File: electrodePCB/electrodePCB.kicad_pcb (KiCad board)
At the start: 2 copper layers, 58 x 58 mm, 17 parts, among them J1 Conn_01x16_Pin, U1 TMP119AIYBGR

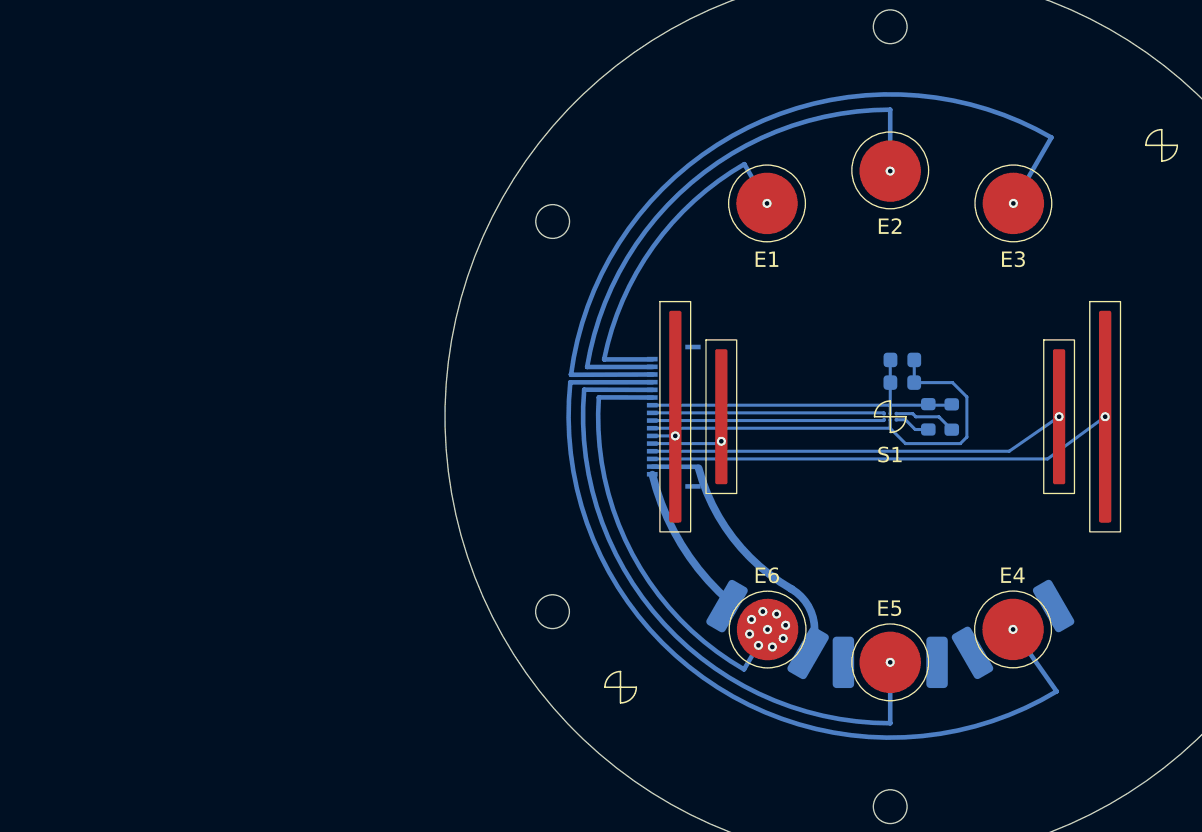
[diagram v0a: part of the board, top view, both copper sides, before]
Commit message: still in the middle of it, but added the 20p, 2 additional heaters (including adjustable postition) and begining to define pinout
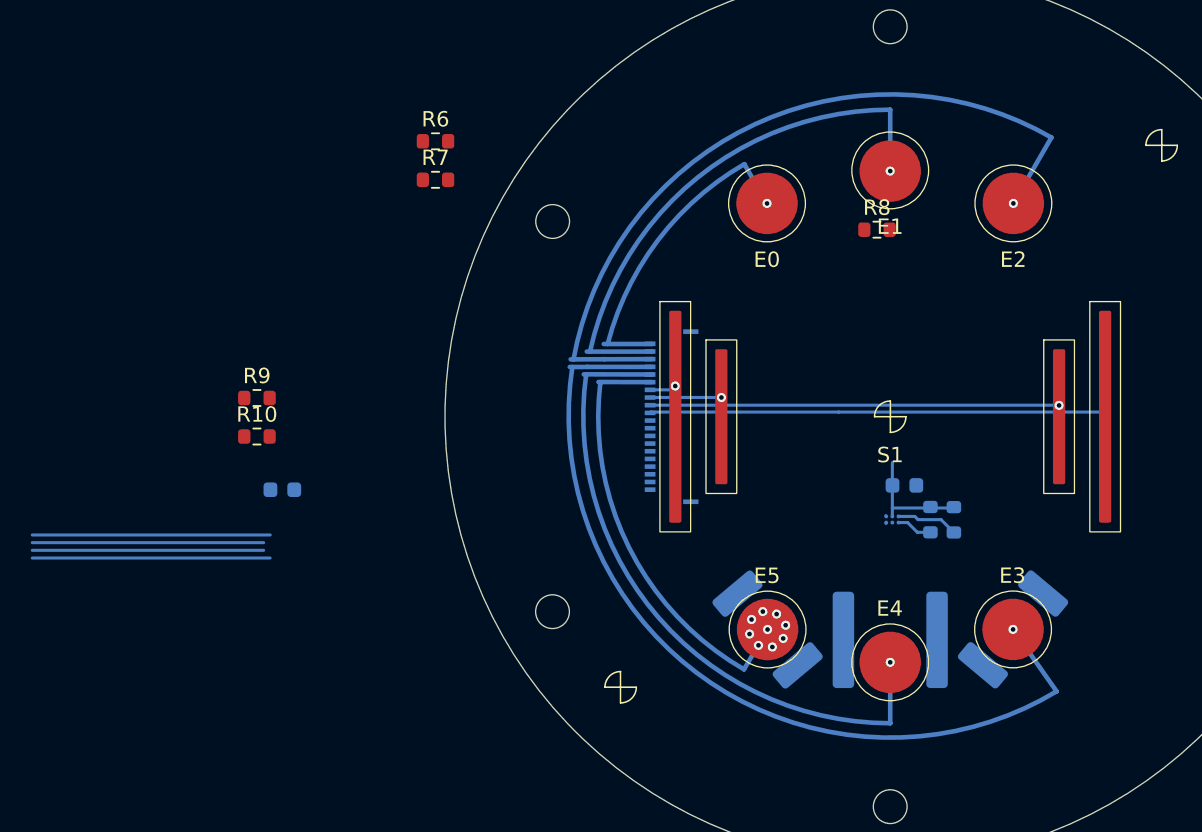
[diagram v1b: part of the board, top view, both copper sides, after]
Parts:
- removed the R1 at (100.0, 116.0)
- removed the R1 at (108.0, 113.9)
- added R10: R_US, Resistor_SMD:R_0603_1608Metric, F.Cu at (58.7, 101.3)
- added R2: R_Small_US, Resistor_SMD:adjustable, B.Cu at (100.0, 116.0)
- added R3: R_Small_US, Resistor_SMD:R_2512_6332Metric_Pad1.40x3.35mm_HandSolder, B.Cu at (108.0, 113.9)
- added R6: R_US, Resistor_SMD:R_0603_1608Metric, F.Cu at (70.4, 82.1)
- added R7: R_US, Resistor_SMD:R_0603_1608Metric, F.Cu at (70.4, 84.6)
- added R8: R_US, Resistor_SMD:R_0603_1608Metric, F.Cu at (99.1, 87.8)
- added R9: R_US, Resistor_SMD:R_0603_1608Metric, F.Cu at (58.7, 98.8)
- J1: value Conn_01x16_Pin -> Conn_01x20; footprint MOLEX FPC:CON_5034801600_MOL -> 5034802000 FPC Molex:CON_5034802000_MOL
- moved C2 41.3 mm to (60.4, 104.8)
- moved C1 6.70 mm to (100.9, 104.5)
- moved R4 6.70 mm to (102.6, 106.7)
- moved R5 6.70 mm to (104.1, 106.7)
- moved U1 6.70 mm to (100.1, 106.7)
- moved J1 0.14 mm to (85.9, 100.0)
- turned R1 to -50 degrees
- renumbered E1 to E0, E2 to E1, E3 to E2, E4 to E3, E5 to E4, E6 to E5, R3 to R4, R2 to R5
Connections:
- J1 pad 10: GND -> Net-(J1-Pin_10)
- J1 pad 11: Net-(J1-Pin_11) -> +3V3
- J1 pad 12: Net-(J1-Pin_12) -> SDA
- J1 pad 13: Net-(J1-Pin_13) -> SCL
- J1 pad 14: Net-(J1-Pin_14) -> GND
- J1 pad 15: Net-(J1-Pin_15) -> GND
- J1 pad 7: +3V3 -> Net-(J1-Pin_7)
- J1 pad 8: SDA -> Net-(J1-Pin_8)
- J1 pad 9: SCL -> Net-(J1-Pin_9)
- R1 pad 1: Net-(J1-Pin_15) -> Net-(J1-Pin_20)
- R1 pad 2: Net-(J1-Pin_16) -> GND
- S1 pad 1: Net-(J1-Pin_11) -> Net-(J1-Pin_7)
- S1 pad 2: Net-(J1-Pin_12) -> Net-(J1-Pin_8)
- S1 pad 3: Net-(J1-Pin_13) -> Net-(J1-Pin_9)
- S1 pad 4: Net-(J1-Pin_14) -> Net-(J1-Pin_10)
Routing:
- net Net-(J1-Pin_14): track 30.4 -> 0.00 mm, vias 1 -> 0
- net Net-(J1-Pin_10): track 0.00 -> 29.7 mm
- net Net-(J1-Pin_13): track 27.2 -> 0.00 mm, vias 1 -> 0
- net Net-(J1-Pin_9): track 0.00 -> 26.6 mm, vias 0 -> 1
- net GND: track 29.5 -> 15.5 mm
- net Net-(J1-Pin_8): track 0.00 -> 4.64 mm, vias 0 -> 1
- net Net-(J1-Pin_12): track 4.56 -> 0.00 mm, vias 1 -> 0
- net Net-(J1-Pin_7): track 0.00 -> 1.64 mm, vias 0 -> 1
- net Net-(J1-Pin_11): track 1.50 -> 0.00 mm, vias 1 -> 0

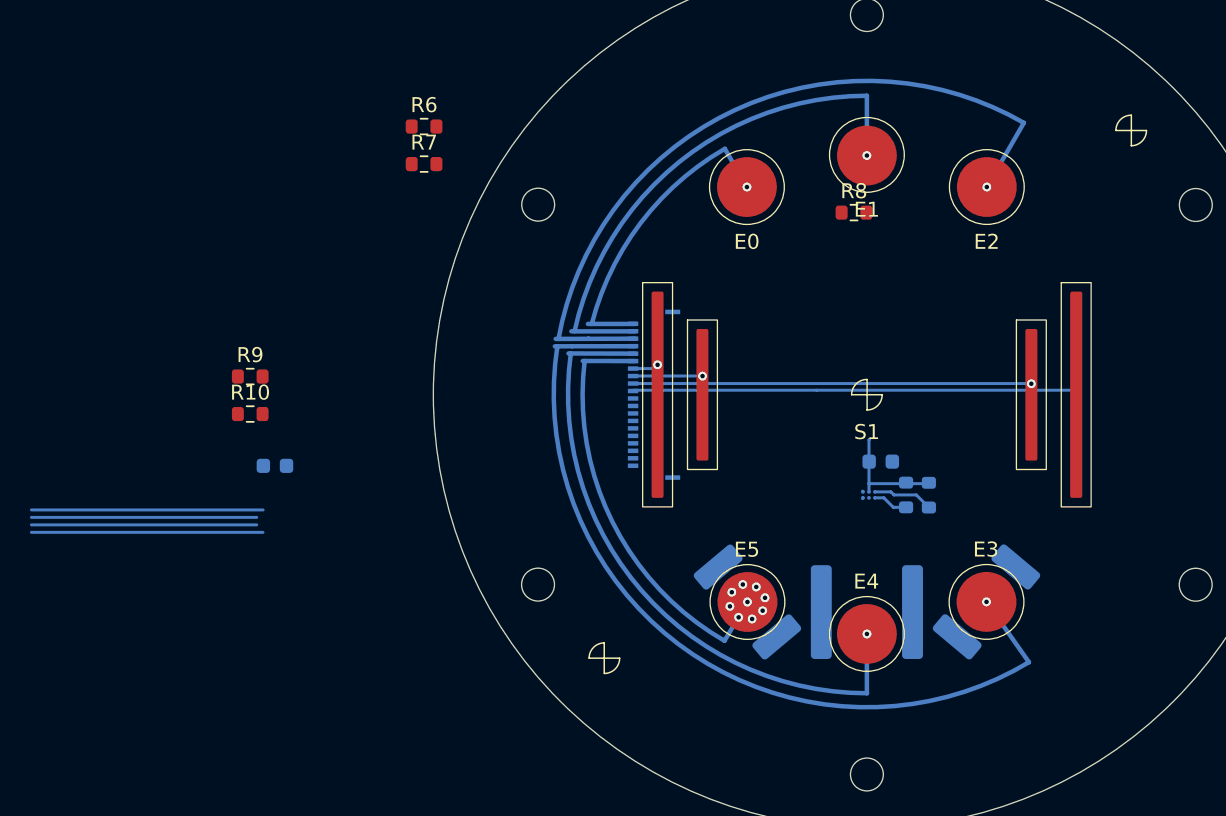
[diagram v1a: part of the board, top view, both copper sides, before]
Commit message: bunch of routing, adapted interconnect pinout to accomedate routing. Added GND plane.
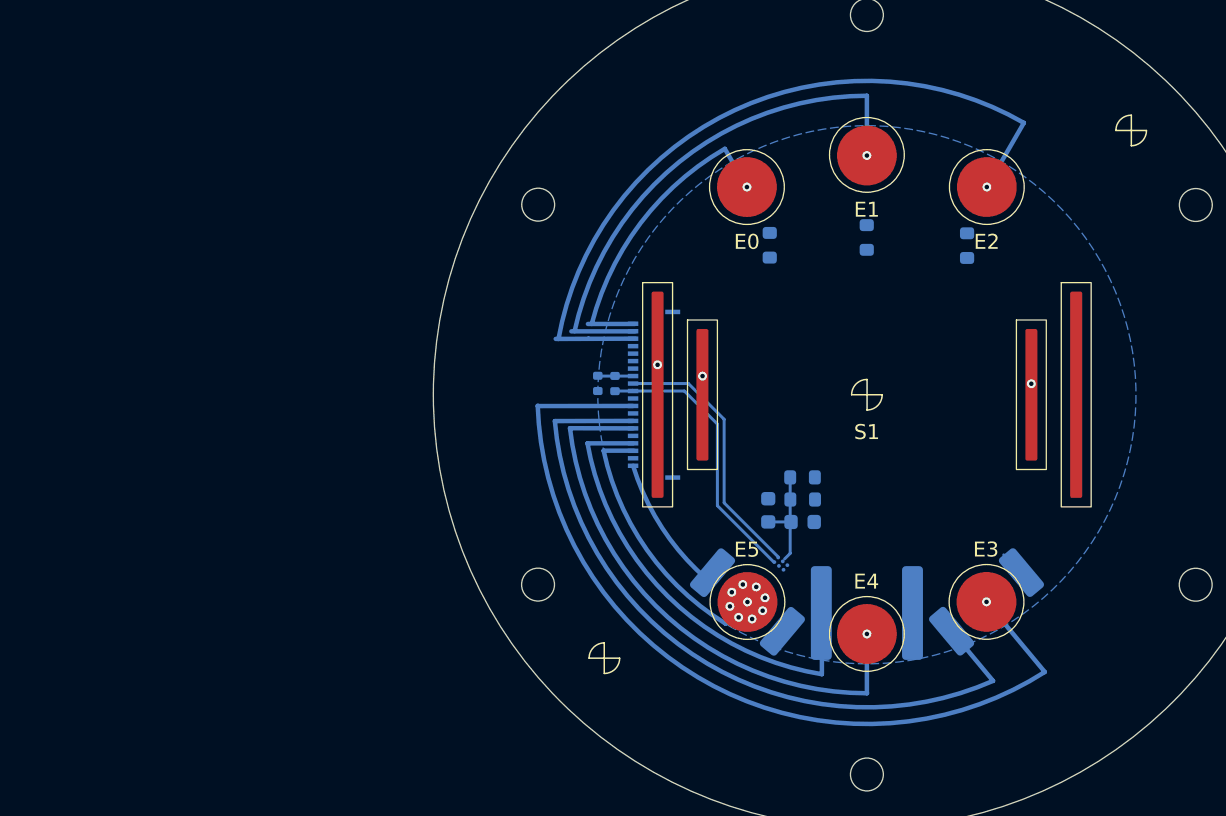
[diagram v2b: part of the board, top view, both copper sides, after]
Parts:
- R10, R8, R9: moved to B.Cu
- R6, R7: footprint Resistor_SMD:R_0603_1608Metric -> Resistor_SMD:R_0402_1005Metric; moved to B.Cu
- moved R10 49.3 mm to (106.7, 90.0), turned to 90 degrees
- moved R9 42.3 mm to (100.0, 89.5), turned to 90 degrees
- moved C2 33.1 mm to (93.4, 107.7), turned to 90 degrees
- moved R6 21.4 mm to (83.2, 99.2), turned to 90 degrees
- moved R7 18.7 mm to (82.0, 99.2), turned to -90 degrees
- moved R5 8.45 mm to (95.7, 107.0), turned to 0 degrees
- moved U1 7.48 mm to (94.2, 111.3), turned to -130 degrees
- moved R4 7.02 mm to (95.7, 105.5), turned to 180 degrees
- moved C1 6.60 mm to (95.7, 108.5)
- moved R8 6.04 mm to (93.5, 90.0), turned to 90 degrees
- moved R2 2.86 mm to (100.0, 113.1), turned to 0 degrees
- turned R1 to -40 degrees
- turned R3 to 40 degrees
- turned REF** to 10 degrees
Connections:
- J1 pad 10: Net-(J1-Pin_10) -> SCL
- J1 pad 11: +3V3 -> GND
- J1 pad 12: SDA -> Net-(E3-Pin_1)
- J1 pad 13: SCL -> GND
- J1 pad 14: GND -> Net-(J1-Pin_14)
- J1 pad 15: GND -> Net-(E4-Pin_1)
- J1 pad 16: Net-(J1-Pin_16) -> GND
- J1 pad 17: GND -> Net-(J1-Pin_17)
- J1 pad 18: Net-(J1-Pin_18) -> Net-(E5-Pin_1)
- J1 pad 4: Net-(E3-Pin_1) -> Net-(J1-Pin_4)
- J1 pad 5: Net-(E4-Pin_1) -> Net-(J1-Pin_5)
- J1 pad 6: Net-(E5-Pin_1) -> Net-(J1-Pin_6)
- J1 pad 8: Net-(J1-Pin_8) -> +3V3
- J1 pad 9: Net-(J1-Pin_9) -> SDA
- R1 pad 1: Net-(J1-Pin_20) -> Net-(J1-Pin_14)
- R2 pad 1: Net-(J1-Pin_18) -> Net-(J1-Pin_17)
- R3 pad 1: Net-(J1-Pin_16) -> Net-(J1-Pin_20)
- S1 pad 1: Net-(J1-Pin_7) -> Net-(J1-Pin_4)
- S1 pad 2: Net-(J1-Pin_8) -> Net-(J1-Pin_5)
- S1 pad 3: Net-(J1-Pin_9) -> Net-(J1-Pin_6)
- S1 pad 4: Net-(J1-Pin_10) -> Net-(J1-Pin_7)
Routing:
- net Net-(J1-Pin_10): track 29.7 -> 0.00 mm
- net Net-(J1-Pin_9): track 26.6 -> 0.00 mm, vias 1 -> 0
- net GND: track 15.5 -> 1.68 mm
- net +3V3: track 23.0 -> 9.53 mm
- net Net-(J1-Pin_8): track 4.64 -> 0.00 mm, vias 1 -> 0
- net Net-(U1-ADD0): track 4.04 -> 0.00 mm
- net SCL: track 15.1 -> 18.6 mm
- net SDA: track 15.1 -> 17.5 mm
- net Net-(U1-ALERT): track 2.34 -> 0.00 mm
- net Net-(J1-Pin_7): track 1.64 -> 0.00 mm, vias 1 -> 0
- net Net-(J1-Pin_6): vias 0 -> 1
- net Net-(J1-Pin_4): vias 0 -> 1
- net Net-(J1-Pin_5): vias 0 -> 1
- added copper zone on B.Cu, net GND

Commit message: routing, routing, routing. We removed one of the three heaters and decided to displace the other two and route to rings around the electrodes. I verified the temperature sensor is work!
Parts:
- removed REF**: thermal_pad, Electrodes:thermal_pad
- added J2: qwiic, Connector_JST:JST_SH_BM04B-SRSS-TB_1x04-1MP_P1.00mm_Vertical, B.Cu at (72.4, 121.6)
- J1: value Conn_01x20 -> FPC 20p
- R1, R3: footprint Resistor_SMD:R_2512_6332Metric_Pad1.40x3.35mm_HandSolder -> Resistor_SMD:R_2010_5025Metric
- R2: footprint Resistor_SMD:adjustable -> Resistor_SMD:R_2010_5025Metric; moved to F.Cu
- moved R2 147.7 mm to (3.21, 1.60)
- moved U1 18.4 mm to (106.2, 97.4)
- moved R5 10.4 mm to (104.3, 101.1)
- moved R4 9.59 mm to (101.7, 98.0)
- moved C1 7.88 mm to (97.4, 100.8), turned to 90 degrees
- moved C2 7.38 mm to (95.9, 100.8)
- moved R3 3.96 mm to (105.6, 110.7)
- moved R1 3.84 mm to (94.5, 110.9)
- moved R9 3.54 mm to (100.8, 86.0), turned to 180 degrees
- moved R8 2.62 mm to (93.7, 87.4), turned to -150 degrees
- moved R10 2.06 mm to (107.8, 88.2), turned to 150 degrees
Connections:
- J1 pad 12: Net-(E3-Pin_1) -> unconnected-(J1-Pin_12-Pad12)
- J1 pad 13: GND -> unconnected-(J1-Pin_13-Pad13)
- J1 pad 14: Net-(J1-Pin_14) -> Net-(E3-Pin_1)
- J1 pad 15: Net-(E4-Pin_1) -> GND
- J1 pad 16: GND -> Net-(J1-Pin_16)
- J1 pad 17: Net-(J1-Pin_17) -> Net-(E4-Pin_1)
- J1 pad 18: Net-(E5-Pin_1) -> Net-(J1-Pin_18)
- J1 pad 20: Net-(J1-Pin_20) -> Net-(E5-Pin_1)
- R1 pad 1: Net-(J1-Pin_14) -> Net-(J1-Pin_18)
- R2 pad 1: Net-(J1-Pin_17) -> Net-(J1-Pin_18)
- R3 pad 1: Net-(J1-Pin_20) -> Net-(J1-Pin_16)
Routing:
- net SDA: track 17.5 -> 3.43 mm
- net SCL: track 18.6 -> 4.72 mm
- net Net-(E4-Pin_1): track 0.00 -> 6.02 mm
- net +3V3: track 9.53 -> 3.90 mm
- net GND: track 1.68 -> 0.02 mm
- net Net-(E5-Pin_1): vias 9 -> 1

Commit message: routing and more routing. still working, but add thermal rings. added qwiic.
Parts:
- removed C2: 10uF, Capacitor_SMD:C_0603_1608Metric
- R4, R5: footprint Resistor_SMD:R_0603_1608Metric -> Resistor_SMD:R_0402_1005Metric
- moved J2 44.4 mm to (113.5, 104.8), turned to 70 degrees
- moved R6 33.9 mm to (116.4, 105.9), turned to -110 degrees
- moved R7 27.2 mm to (108.9, 103.2), turned to 70 degrees
- moved U1 19.6 mm to (100.0, 116.0), turned to 0 degrees
- moved R4 17.5 mm to (98.8, 115.3), turned to -95 degrees
- moved R5 16.0 mm to (96.2, 114.9), turned to 75 degrees
- moved C1 13.9 mm to (97.6, 114.7), turned to 80 degrees
- moved J1 3.14 mm to (89.0, 100.0)
- moved R1 0.67 mm to (94.0, 110.4), turned to -30 degrees
- moved R3 0.49 mm to (106.0, 110.4), turned to 30 degrees
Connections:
- J1 pad 10: SCL -> +3V3
- J1 pad 8: +3V3 -> SCL
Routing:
- net SCL: track 4.72 -> 36.3 mm
- net +3V3: track 3.90 -> 33.4 mm
- net Net-(J1-Pin_7): track 0.00 -> 27.2 mm, vias 0 -> 1
- net SDA: track 3.43 -> 29.9 mm
- net Net-(J1-Pin_6): track 0.00 -> 23.5 mm
- net Net-(U1-ADD0): track 0.00 -> 4.36 mm
- net Net-(E0-Pin_1): track 0.00 -> 3.65 mm
- net Net-(E4-Pin_1): track 6.02 -> 3.65 mm
- net Net-(U1-ALERT): track 0.00 -> 1.72 mm
- net Net-(J1-Pin_5): track 0.00 -> 1.60 mm
- added copper zone on B.Cu, net (none)
- added copper zone on F.Cu, net (none)
- added copper zone on F.Cu, net unconnected-(J2-MountPin-PadMP)

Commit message: roughly finalized layout. Might tidy up the GND plane with some keep outs
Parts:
- removed the R2 at (3.21, 1.60)
- R1: renamed from R7; value R_US -> 10k
- R2: renamed from R6; value R_US -> 10k
- R4: value R_US -> 10k
- R6: renamed from R5; value R_US -> 10k
- renumbered R1 to R5, R8 to R7, R9 to R8, R10 to R9
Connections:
- J1 pad 12: unconnected-(J1-Pin_12-Pad12) -> Net-(E3-Pin_1)
- J1 pad 13: unconnected-(J1-Pin_13-Pad13) -> Net-(J1-Pin_13)
- J1 pad 14: Net-(E3-Pin_1) -> Net-(J1-Pin_13)
- J1 pad 16: Net-(J1-Pin_16) -> Net-(E4-Pin_1)
- J1 pad 17: Net-(E4-Pin_1) -> Net-(J1-Pin_17)
- J1 pad 18: Net-(J1-Pin_18) -> Net-(J1-Pin_17)
- J1 pad P1: (no net) -> GND
- J1 pad P2: (no net) -> GND
- R3 pad 1: Net-(J1-Pin_16) -> Net-(J1-Pin_13)
- R5 pad 1: Net-(J1-Pin_18) -> Net-(J1-Pin_17)
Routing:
- net Net-(U1-ADD0): track 4.36 -> 3.82 mm
- net E5_therm_pad: vias 0 -> 3
- net E3_therm_pad: vias 0 -> 3
- added copper zone on B.Cu, net E3_therm_pad
- added copper zone on F.Cu, net E3_therm_pad
- added copper zone on B.Cu, net E5_therm_pad
- added copper zone on F.Cu, net E5_therm_pad
- removed copper zone on B.Cu, net (none)
- removed copper zone on F.Cu, net (none)
- removed copper zone on F.Cu, net unconnected-(J2-MountPin-PadMP)

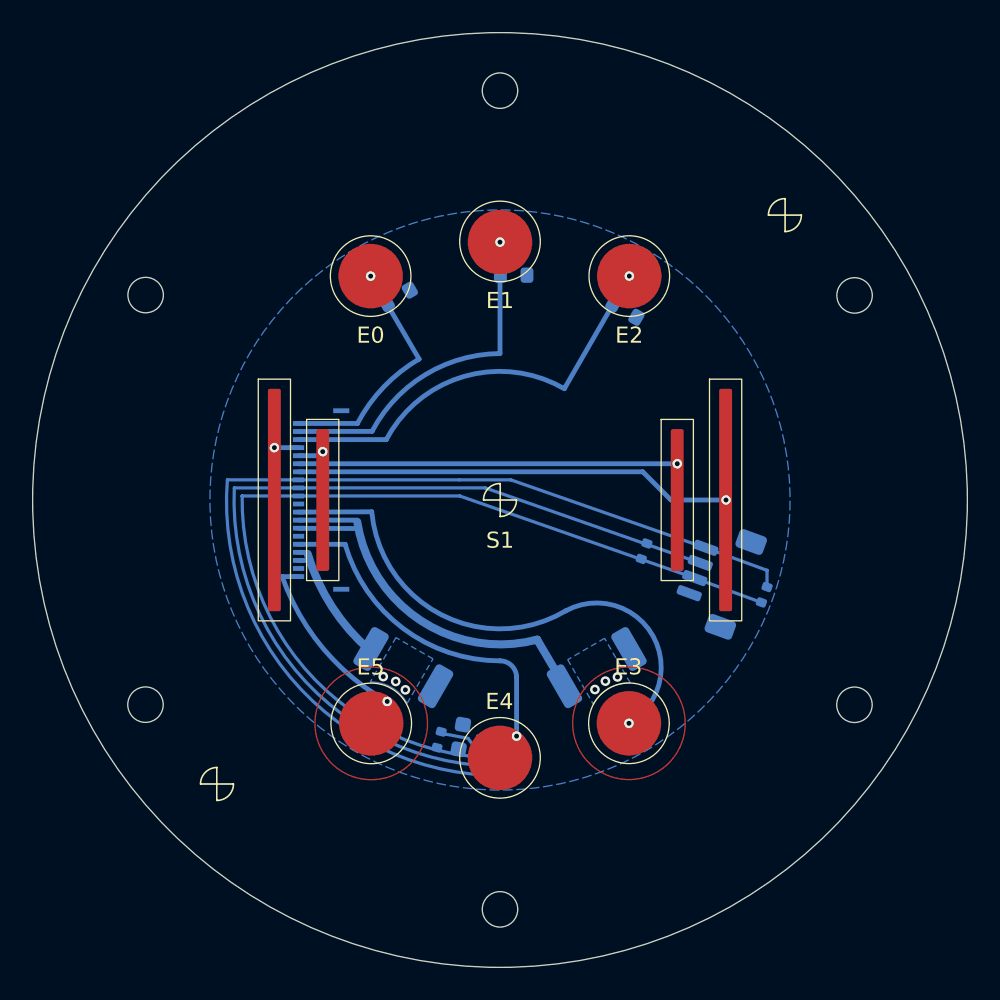
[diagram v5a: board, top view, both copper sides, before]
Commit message: added releifs for screws so we do not have to completely remove them
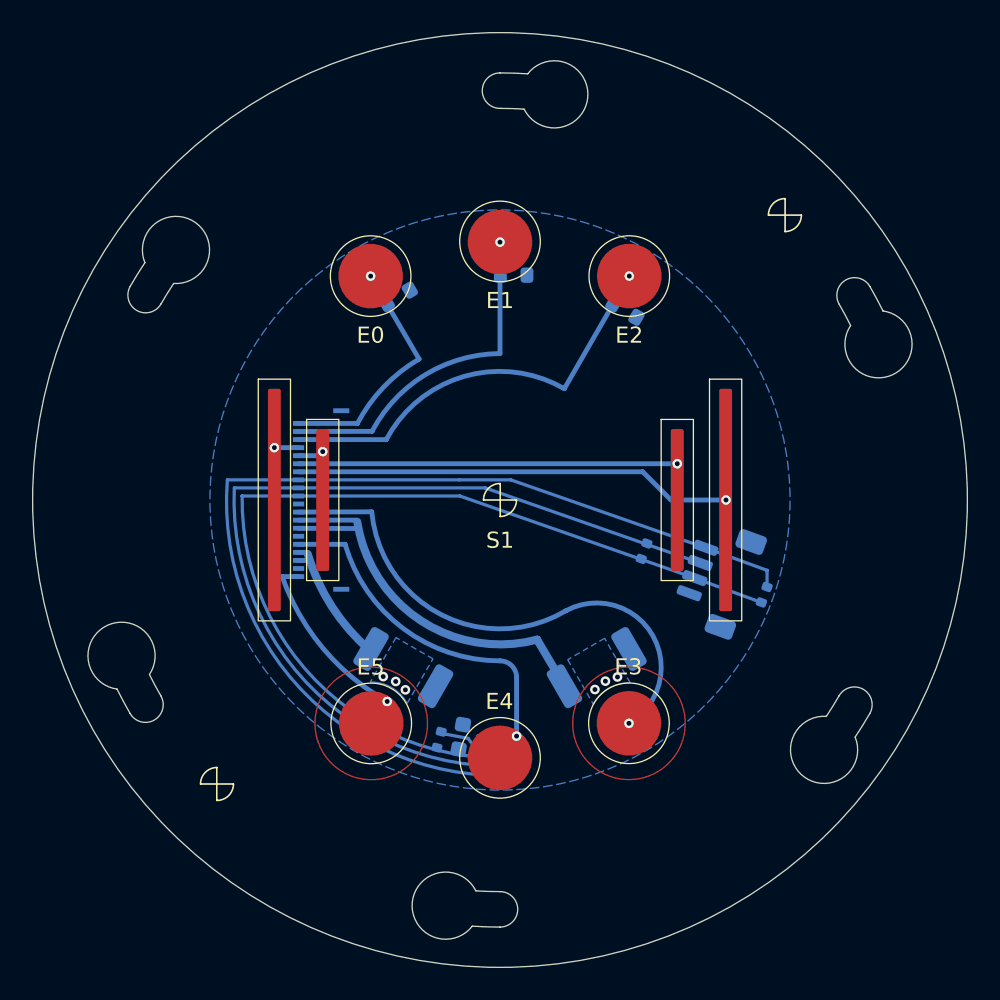
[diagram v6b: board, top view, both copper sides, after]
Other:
- outline, holes or cut-outs redrawn
